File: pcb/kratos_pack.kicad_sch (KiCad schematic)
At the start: 97 parts, among them J1 USB_C_Receptacle_USB2.0, J2 PROG_CONN, J3 DBG_UART, J4 BAT_MID+NTC, J5 BAT_7.4V, J6 BAT_0V, J7 OUT+, J8 OUT-, Q1 AON7403, Q2 AON7414, Q3 AON7414, SW1 WAKEUP, SW2 BOOT, SW3 RST_BTN, U1 USBLC6-2SC6, U10 24LC32, U2 CP2102N-Axx-xQFN20, U3 STM32G071Gx, U4 KTD2026BEWE, U5 BQ25887, U6 BD48xxFVE, U7 INA199, U8 LTC4231, U9 LDK715M33R

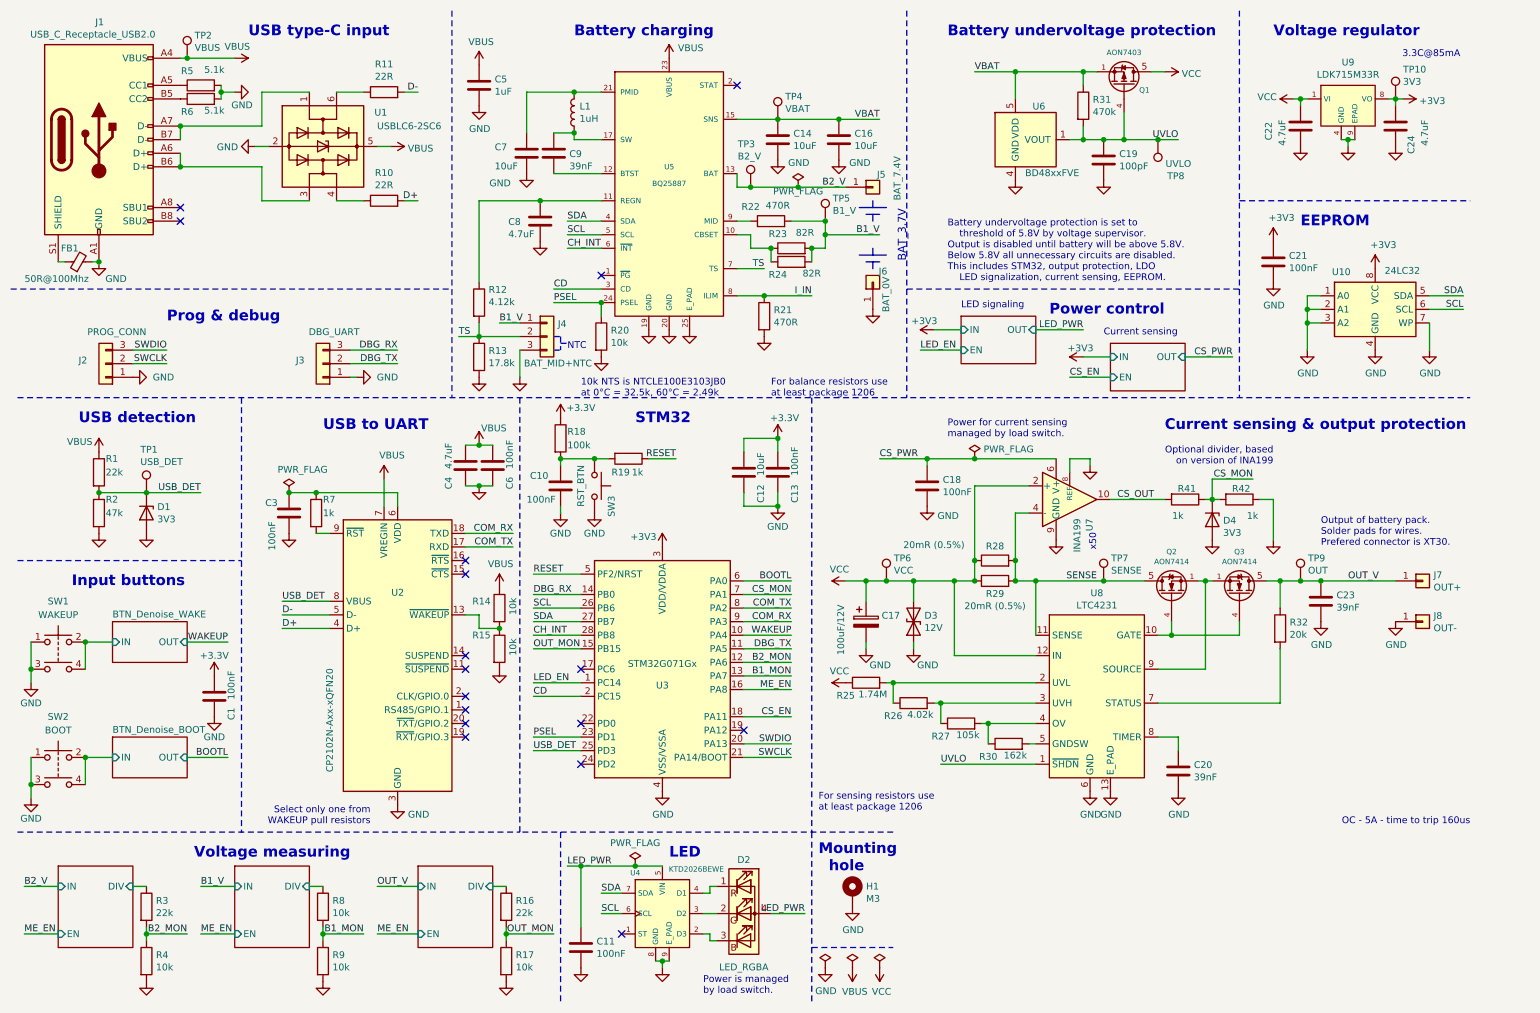
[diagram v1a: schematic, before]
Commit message: PCB: connector mounting point to ground, change LDk package to SOT-23-5
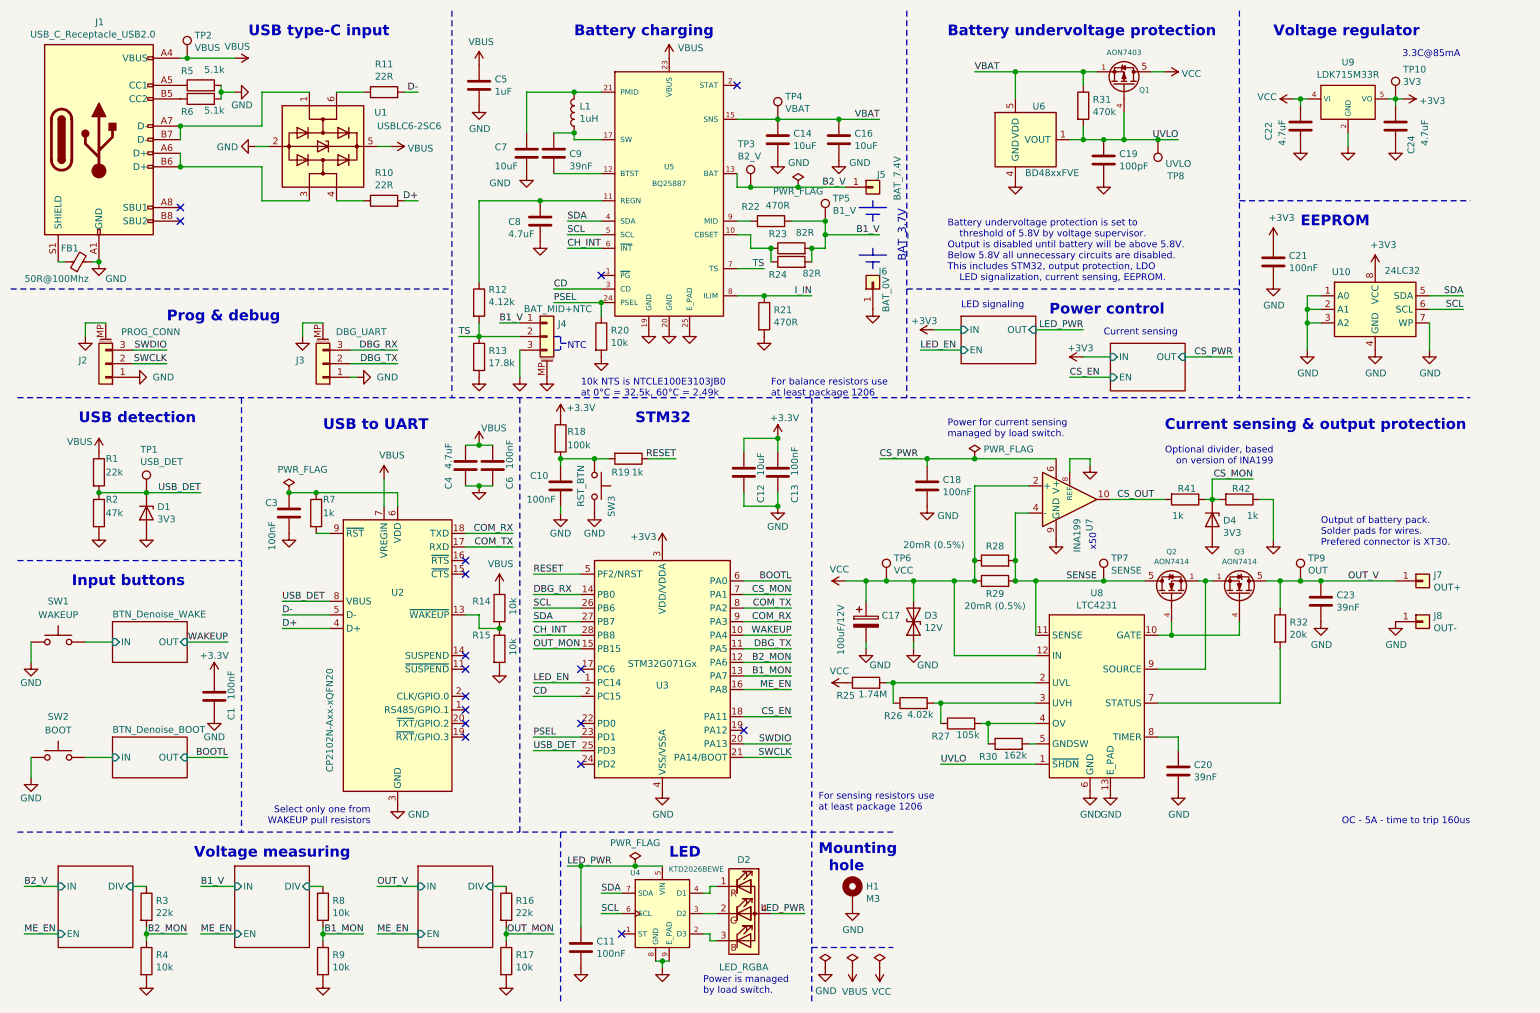
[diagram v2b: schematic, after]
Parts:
- J2, J3, J4: symbol Connector_Generic:Conn_01x03 -> Connector_Generic_MountingPin:Conn_01x03_MountingPin
- SW1, SW2: symbol Switch:SW_Push_Dual -> Switch:SW_Push
- U9: footprint Package_DFN_QFN:DFN-8-1EP_3x3mm_P0.65mm_EP1.7x2.05mm -> Package_TO_SOT_SMD:SOT-23-5; symbol TCY_IC:LDK715M33R -> TCY_voltage_regulators:LDK715M33R
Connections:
- net +3V3: now also U9.5 (VO); no longer U9.8 (VO)
- net BTN_Denoise_BOOT/IN: no longer SW2.4
- net BTN_Denoise_WAKE/IN: no longer SW1.4
- net GND: now also J2.MP (MountPin), J3.MP (MountPin), J4.MP (MountPin), U9.2 (GND); no longer SW1.3, SW2.3, U9.4 (GND), U9.9 (EPAD)
- net VCC: now also U9.4 (VI); no longer U9.1 (VI)

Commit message: PCB: update page layout and update to new version
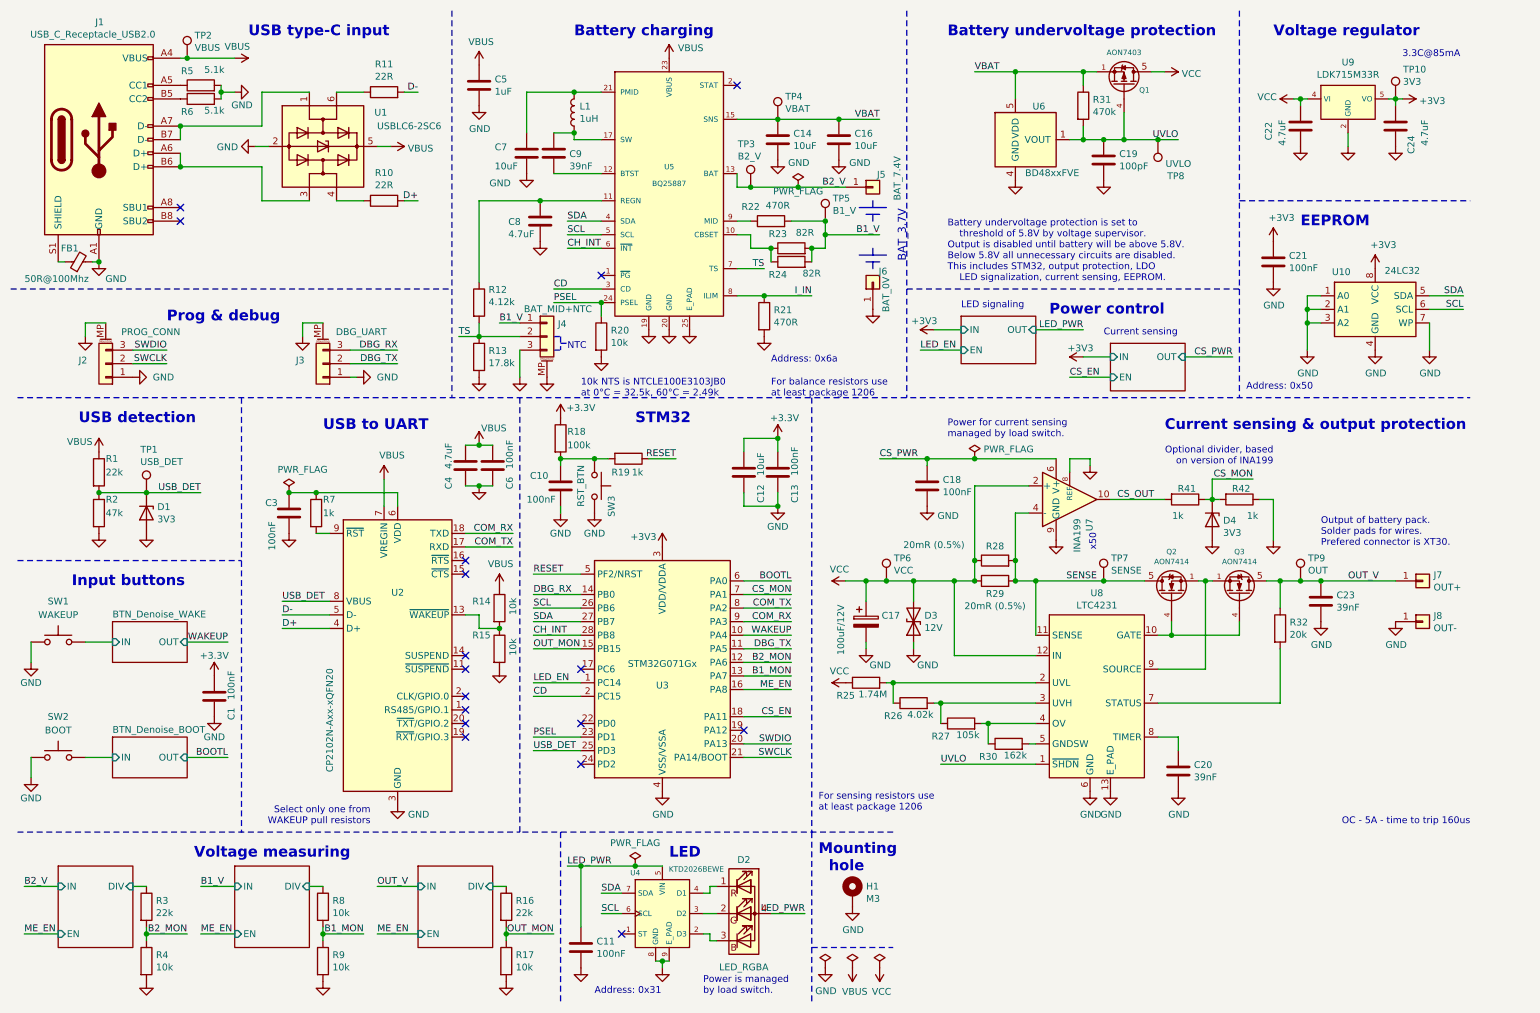
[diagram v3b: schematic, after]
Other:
- note added: "Address: 0x31"
- note added: "Address: 0x50"
- note added: "Address: 0x6a"
